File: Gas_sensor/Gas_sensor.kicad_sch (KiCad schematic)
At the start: 90 parts

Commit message: update gaz sensor sch
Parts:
- removed SW?: SW_MEC_5E, symbol Switch:SW_MEC_5E
- added C1, C33, C34, C36, C37, C38: 100n, symbol Device:C
- added J2: Conn_01x04, symbol Connector_Generic:Conn_01x04
- added J3: Conn_01x10, symbol Connector_Generic:Conn_01x10
- added Q4: Q_NMOS_GSD, symbol Device:Q_NMOS_GSD
- added R17, R18, R19, R20: 2.2k, symbol Device:R
- added R21, R22, R23, R26, R27, R28: 0, symbol Device:R
- added R29, R30, R31, R32, R33, R34, R35, R36: 390k, symbol Device:R
- added R38, R39, R45, R46, R47: 100k, symbol Device:R
- added R43, R44, R52, R53, R54: 3.9k, symbol Device:R
- added SW1, SW2, SW3, SW5: SW_MEC_5G, symbol Switch:SW_MEC_5G
- added U1: LPV511, Package_TO_SOT_SMD:SOT-23-5, symbol Amplifier_Operational:LPV811DBV
- C11, C14, C15, C22, C27, C28, C29, C3, C30, C31, C5, C7, C8: renamed from C?; value C -> 100n
- C12, C13: renamed from C?; value C -> 100p
- C16, C17, C18: renamed from C?; value C -> 1u
- C9: renamed from C?; value C -> 10u
- Q1, Q2: renamed from Q?; value DUAL_MOS_QFN -> PMCXB900UE
- R1, R2, R7, R9: renamed from R?; value R -> 0
- R11, R12, R13: renamed from R?; value R -> 100
- gave numbers to parts that had none: 59
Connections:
- net +3V3: now also C1.1, J2.1 (Pin_1), R17.1, R18.1, R19.1, R29.1, R31.1, R33.1, R35.1, R43.1, R44.1, R52.1, R53.1, R54.1, U1.5 (V+)
- net +9V: now also R20.1
- net GND: now also SW4.3 (B), SW4.4 (B), C1.2, C33.2, C34.2, C36.2, C37.2, C38.2, J2.4 (Pin_4), Q4.2 (S), R30.2, R32.2, R34.2, R36.2, SW1.3 (B), SW1.4 (B), SW2.3 (B), SW2.4 (B), SW3.3 (B), SW3.4 (B), SW5.3 (B), SW5.4 (B), U1.2 (V-)
- net SCL: now also U11.42 (PB6), R19.2
- net SDA: now also U11.43 (PB7), R17.2
- net Vheater: now also R12.1, R15.2, R16.1; no longer C12.1, R7.2
- net Vsensor: now also R11.1, U7.1, U7.4 (-); no longer C13.1, R9.2
- net Isensor: now reaches U2.3 (+)
- net Isensor: now also C13.1, R9.2
- net Vheater_EN: now reaches Q3.1 (G)
- net Vheater_EN: now also U11.29 (PA8)
- net at BZ1.1: now also R18.2, R20.2
- net at BZ1.2: now also Q4.3 (D)
- net SenseBatt_EN: now reaches Q5.1 (G)
- net SenseBatt_EN: now also U11.17 (PA7)
- net ADC1: now reaches C17.1, R12.2
- net ADC1: now also R22.1, R27.2; no longer U9.5 (AIN1)
- net ADC2: now reaches C18.1, R13.2
- net ADC2: now also R23.1, R26.2; no longer U9.6 (AIN2)
- net at U3.2 (Vref0): now also U1.3 (+)
- net at U3.5 (Vout1): now also R7.1
- net ADC0: now reaches C16.1, R11.2
- net ADC0: now also R21.1, R28.2; no longer U9.4 (AIN0)
- net SenseBatt: now reaches R41.2, R42.1
- net SenseBatt: now also R13.1
- net Vseg0: now reaches U11.10 (PA0)
- net Vseg0: now also J3.5 (Pin_5)
- net Vseg1: now reaches U11.11 (PA1)
- net Vseg1: now also J3.6 (Pin_6)
- net Vseg2: now reaches U11.12 (PA2)
- net Vseg2: now also J3.7 (Pin_7)
- net Vseg3: now reaches U11.13 (PA3)
- net Vseg3: now also J3.8 (Pin_8)
- net Vseg4: now reaches U11.14 (PA4)
- net Vseg4: now also J3.9 (Pin_9)
- net Vseg5: now reaches U11.15 (PA5)
- net Vseg5: now also J3.10 (Pin_10)
- net at U11.16 (PA6): now also R28.1
- net at U11.18 (PB0): now also R27.1
- net at U11.19 (PB1): now also R26.1
- net Sound: now reaches U11.21 (PB10)
- net Sound: now also C34.1, R39.1
- net High: now reaches U11.25 (PB12)
- net High: now also C36.1, R45.1
- net Mid: now reaches U11.26 (PB13)
- net Mid: now also C37.1, R46.1
- net Low: now reaches U11.27 (PB14)
- net Low: now also C38.1, R47.1
- net PW_ON: now reaches U11.28 (PB15)
- net PW_ON: now also Q6.1 (G), R48.1
- net Vcomm0: now reaches U11.30 (PA9)
- net Vcomm0: now also J3.1 (Pin_1), R29.2, R30.1
- net Vcomm1: now reaches U11.31 (PA10)
- net Vcomm1: now also J3.2 (Pin_2), R31.2, R32.1
- net Vcomm2: now reaches U11.32 (PA11)
- net Vcomm2: now also J3.3 (Pin_3), R33.2, R34.1
- net Vcomm3: now reaches U11.33 (PA12)
- net Vcomm3: now also J3.4 (Pin_4), R35.2, R36.1
- net SWDIO: now reaches U11.34 (PA13)
- net SWDIO: now also J2.2 (Pin_2)
- net SWCLK: now reaches U11.37 (PA14)
- net SWCLK: now also J2.3 (Pin_3)
- net Buzzer_EN: now reaches U11.45 (PB8)
- net Buzzer_EN: now also Q4.1 (G)
- net APO: now reaches U11.46 (PB9)
- net APO: now also C33.1, R38.1
- net Vref_DAC: now reaches U11.9 (VREF+)
- net Vref_DAC: now also U1.1, U1.4 (-)
- net Iheater: now reaches U4.3 (+)
- net Iheater: now also C12.1, R7.2
- net at SW4.1 (A), SW4.2 (A): now also R46.2, R53.2
- new net: R45.2, R52.2, SW3.1 (A), SW3.2 (A)
- new net: R47.2, R54.2, SW5.1 (A), SW5.2 (A)
- new net: R39.2, R44.2, SW2.1 (A), SW2.2 (A)
- new net: R38.2, R43.2, SW1.1 (A), SW1.2 (A)
- new net: R23.2, U9.6 (AIN2)
- new net: R21.2, U9.4 (AIN0)
- new net: R22.2, U9.5 (AIN1)
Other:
- moved on the sheet: BZ1, C16, C17, C18, C21, C22, C23, C25, J4, R11, R12, R13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

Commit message: update gas sensor schematic
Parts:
- removed SW6: SW_MEC_5E, symbol Switch:SW_MEC_5E
- added C41, C42: 100n, Yame_library:SM0201-MR, symbol Device:C
- added C43: 10n, Yame_library:SM0402-MR, symbol Device:C
- added C44, C45: 10u, Yame_library:SM0603-MR, symbol Device:C
- added L2: L_Ferrite, Yame_library:SM0603-MR, symbol Device:L_Ferrite
- added SW6: SW_MEC_5G, Yame_library:SW_CARBON, symbol Switch:SW_MEC_5G
- added U14: TPS79333-EP, Package_TO_SOT_SMD:SOT-23-5, symbol Regulator_Linear:TPS79333-EP
- added U15: REG102GA, Package_TO_SOT_SMD:SOT-223-6, symbol YameLib:REG102GA
- BZ1: footprint (none) -> Buzzer_Beeper:Buzzer_15x7.5RM7.6
- C1, C11, C14, C15, C2, C20, C22, C26, C27, C28, C29, C3, C30, C31, C33, C34, C35, C36, C37, C38, C5, C6, C7, C8: footprint (none) -> Yame_library:SM0201-MR
- C10, C12, C13, C23, C25, C4, R1, R10, R11, R12, R13, R14, R15, R16, R17, R18, R19, R2, R20, R21, R22, R23, R24, R25, R26, R27, R28, R29, R3, R30, R31, R32, R33, R34, R35, R36, R37, R38, R39, R4, R40, R41, R42, R43, R44, R45, R46, R47, R48, R49, R5, R50, R51, R52, R53, R54, R55, R6, R7, R8, R9: footprint (none) -> Yame_library:SM0402-MR
- C16, C17, C18, C19, C21, C24, C32, C39, C9: footprint (none) -> Yame_library:SM0603-MR
- C40: footprint (none) -> Yame_library:SM0805-MR
- J3: footprint (none) -> Yame_library:LCD_Contact_1x10_P2.54mm
- L1: footprint (none) -> Yame_library:L_Bourns-SDR0805_7.8x8mm
- Q1, Q2: value PMCXB900UE -> DMC1229UFDB; footprint Package_SON:Fairchild_DualPower33-6_3x3mm -> Package_DFN_QFN:DFN-6-1EP_2x2mm_P0.65mm_EP1x1.6mm
- Q3, Q4, Q5, Q6: footprint (none) -> Package_TO_SOT_SMD:SOT-23
- SW1: footprint (none) -> Button_Switch_SMD:SW_SPST_EVPBF
- SW2, SW3, SW4, SW5: footprint (none) -> Yame_library:SW_CARBON
- U12: footprint Package_TO_SOT_SMD:SOT-23-6 -> Package_SON:WSON-6-1EP_2x2mm_P0.65mm_EP1x1.6mm_ThermalVias
- U13: footprint Package_SON:Texas_S-PWSON-N10_ThermalVias -> Yame_library:VQFN-HR-15-1EP_3x2.5mm_P0.5m
- U3: footprint (none) -> Package_DFN_QFN:QFN-16-1EP_3x3mm_P0.5mm_EP1.7x1.7mm
- U4, U5: footprint Package_TO_SOT_SMD:SOT-23-5 -> Package_TO_SOT_SMD:SOT-353_SC-70-5
- Y1: footprint (none) -> Oscillator:Oscillator_SMD_Abracon_ASE-4Pin_3.2x2.5mm_HandSoldering
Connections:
- net +3V3: now also C44.1, C45.1, U14.5 (OUT), U15.2 (Vout)
- net +9V: now also U13.7_8 (VOUT); no longer U13.7 (VOUT), U13.8 (VOUT)
- net +BATT: now also U13.13_12 (VIN), C41.1, C42.1, U14.1 (IN), U14.3 (EN), U15.1 (Vin), U15.5 (EN); no longer U13.12 (VIN), U13.13 (VIN)
- net GND: now also U3.17 (EP), C41.2, C42.2, C43.2, C44.2, C45.2, SW6.3 (B), SW6.4 (B), U14.2 (GND), U15.3 (GND), U15.6 (GND_Pad)
- net Vref_DAC: now also L2.1; no longer U11.9 (VREF+)
- net at U3.5 (Vout1): now also R7.1
- net at J5.1 (Pin_1), Q6.2 (S): now also SW6.1 (A), SW6.2 (A)
- new net: L2.2, U11.9 (VREF+)
- new net: C43.1, U14.4 (BP)

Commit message: update sch, start layout
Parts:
- removed SW1: SW_MEC_5G, Button_Switch_SMD:SW_SPST_EVPBF, symbol Switch:SW_MEC_5G
- removed SW2, SW3, SW4, SW5, SW6: SW_MEC_5G, Yame_library:SW_CARBON, symbol Switch:SW_MEC_5G
- added SW1, SW10, SW2, SW5, SW7, SW9: SW_Push, Button_Switch_SMD:SW_SPST_EVPBF, symbol YameLib:SW_Push
- added SW11, SW12, SW3, SW4, SW6, SW8: SW_Push, Yame_library:SW_CARBON, symbol YameLib:SW_Push
- J1, J2: footprint (none) -> Connector_PinHeader_2.54mm:PinHeader_1x04_P2.54mm_Vertical
- J4, J5: footprint (none) -> Yame_library:Conn1_batt
- Q1, Q2: footprint Package_DFN_QFN:DFN-6-1EP_2x2mm_P0.65mm_EP1x1.6mm -> Yame_library:U-DFN2020-6_2x2mm_P0.65mm_EP0.6mm
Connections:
- net GND: now also SW1.2, SW10.2, SW11.2, SW12.2, SW2.2, SW3.2, SW4.2, SW5.2, SW6.2, SW7.2, SW8.2, SW9.2
- net at R45.2, R52.2: now also SW5.1, SW8.1
- net at R47.2, R54.2: now also SW10.1, SW12.1
- net at R39.2, R44.2: now also SW2.1, SW4.1
- net at U3.5 (Vout1): now also R7.1
- net at J5.1 (Pin_1), Q6.2 (S): now also SW6.1, SW7.1
- net at R46.2, R53.2: now also SW11.1, SW9.1
- net at R38.2, R43.2: now also SW1.1, SW3.1
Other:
- moved on the sheet: C33, C34, C36, C37, C38, J4, J5, Q5, Q6, R38, R39, R40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

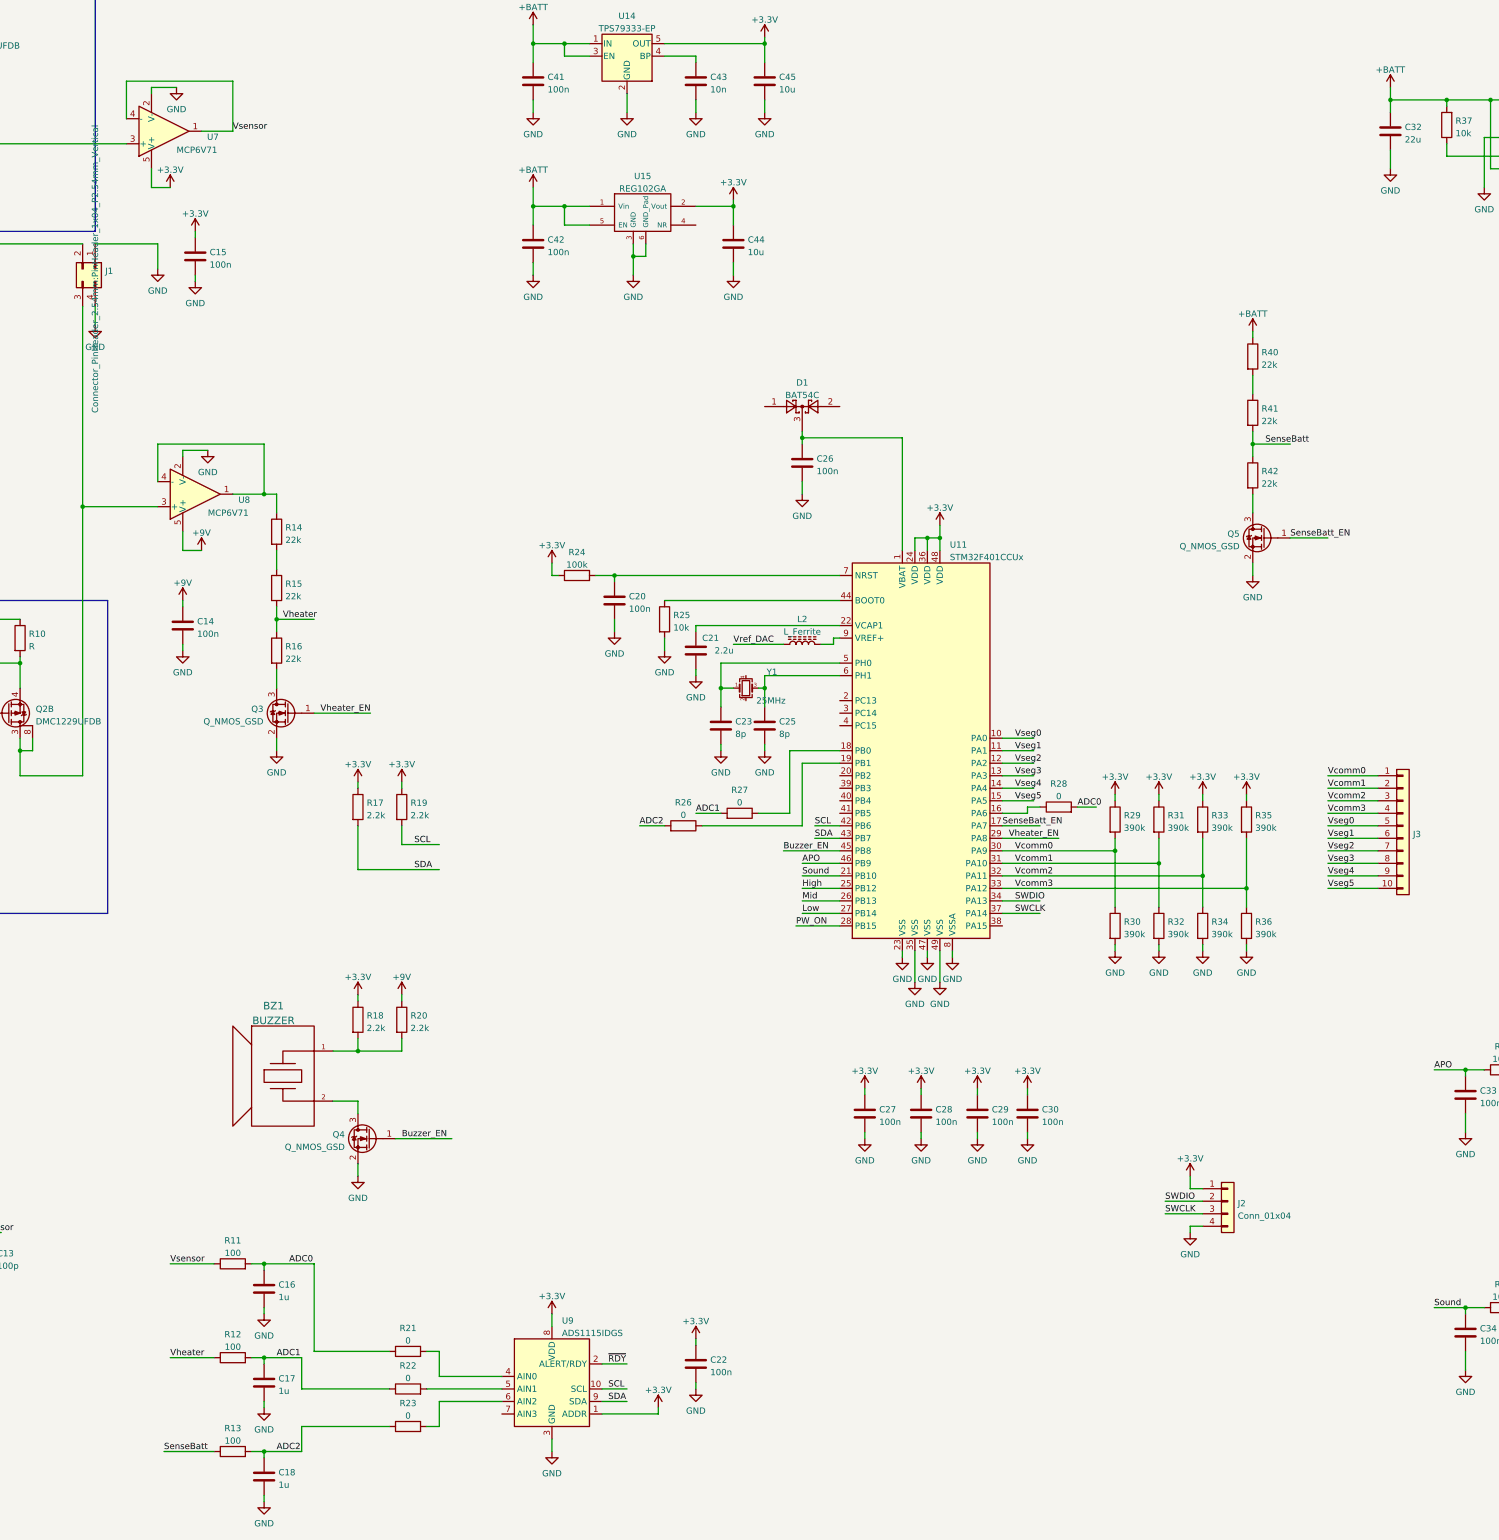
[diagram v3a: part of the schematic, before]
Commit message: Update layout, place switch
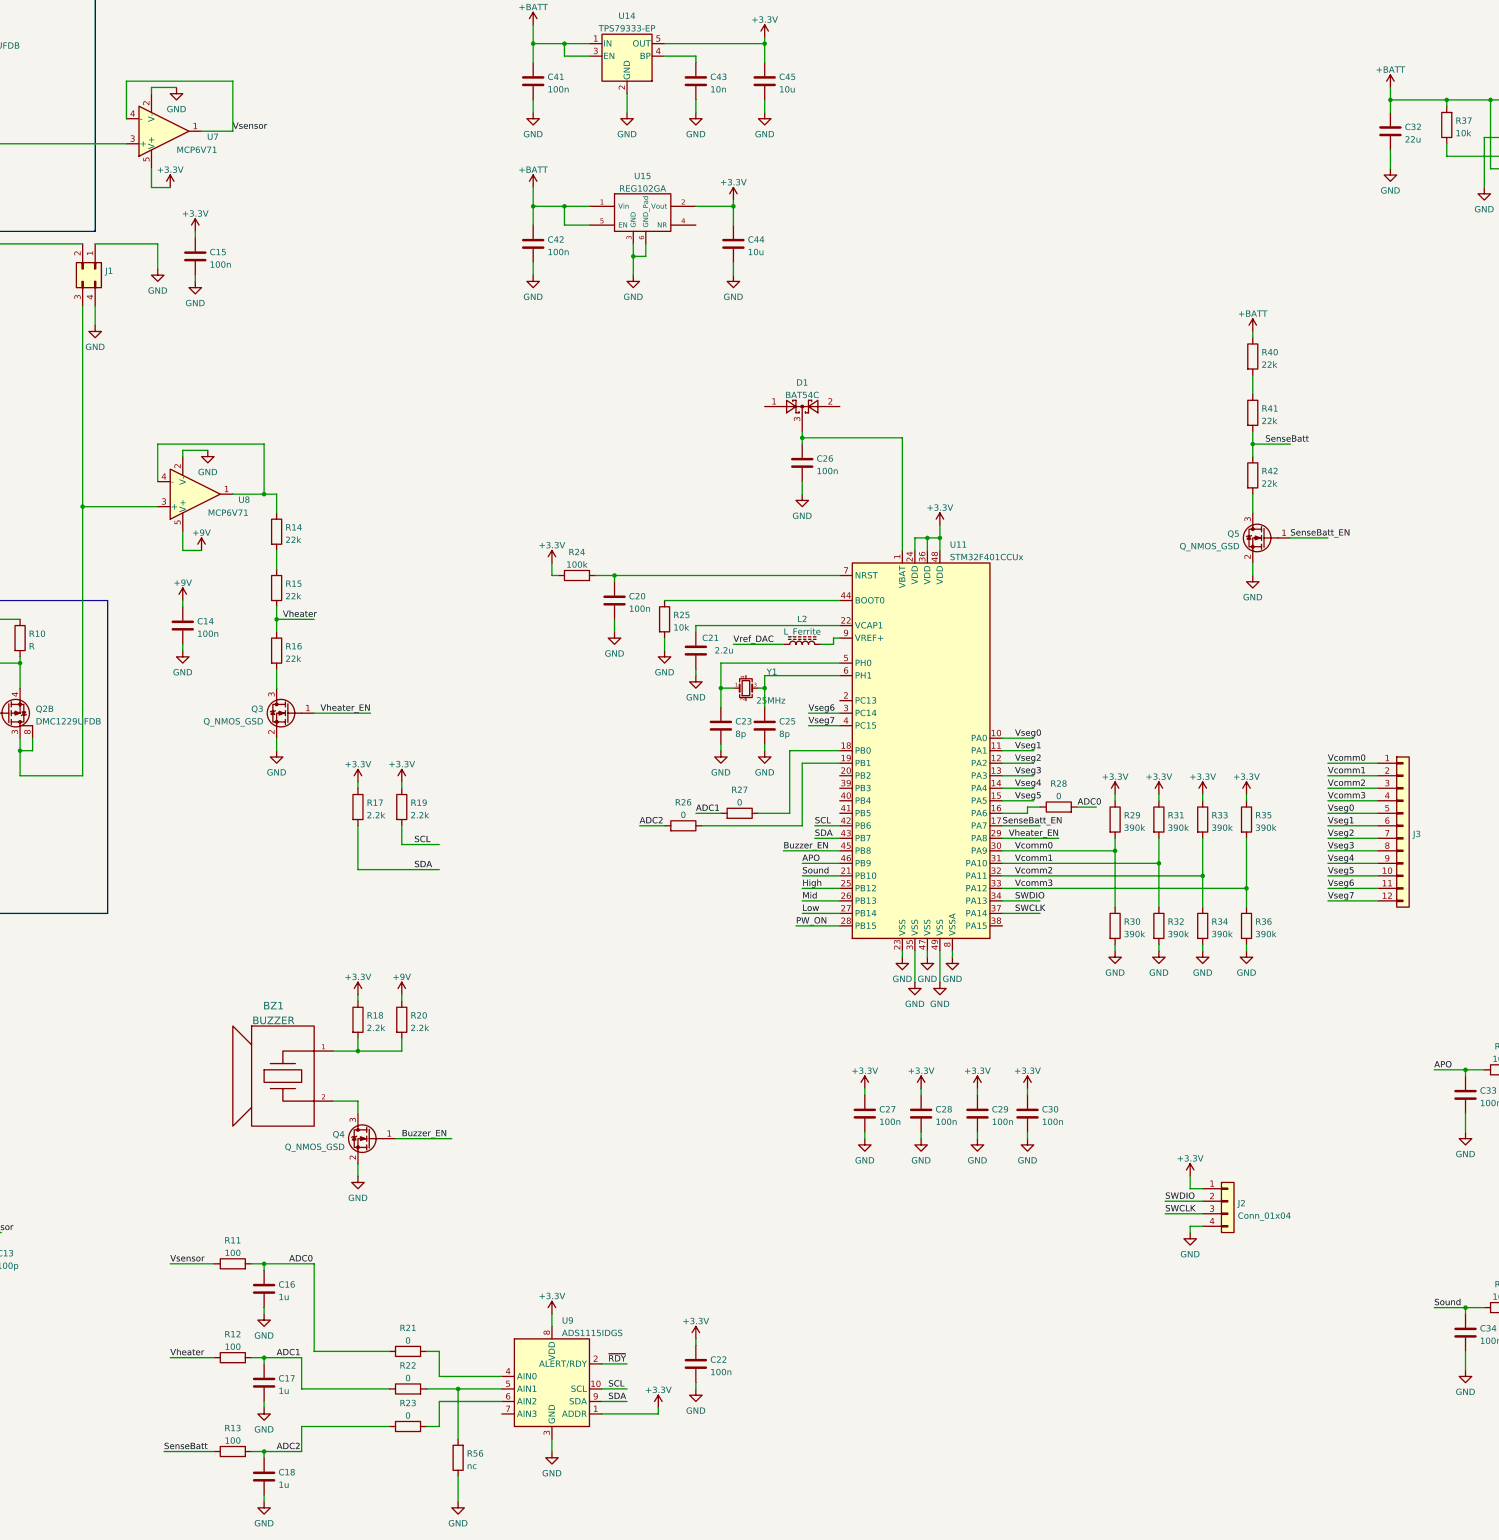
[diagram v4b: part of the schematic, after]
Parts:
- added R56: nc, Yame_library:SM0402-MR, symbol Device:R
- J3: footprint Yame_library:LCD_Contact_1x10_P2.54mm -> Yame_library:LCD_Contact_1x12_P2.54mm; symbol Connector_Generic:Conn_01x10 -> Connector_Generic:Conn_01x12
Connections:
- net GND: now also R56.1
- net at U3.5 (Vout1): now also R7.1
- net at R22.2, U9.5 (AIN1): now also R56.2
- net Vseg6: now reaches U11.3 (PC14)
- net Vseg6: now also J3.11 (Pin_11)
- net Vseg7: now reaches U11.4 (PC15)
- net Vseg7: now also J3.12 (Pin_12)
